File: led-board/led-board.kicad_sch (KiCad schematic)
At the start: 0 parts

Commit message: wip: start LED circuit
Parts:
- added D1: LED, symbol Device:LED
- added R1: R, symbol Device:R
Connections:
- new net: D1.2 (A), R1.1
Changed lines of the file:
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@@
 	(generator_version "10.0")
 	(paper "A4")
+	(title_block
+		(date "2026-04-19")
+		(rev "v0.0.1")
+	)
+	(wire
+		(pts
+			(xy 132.08 82.55) (xy 133.35 82.55)
+		)
+		(stroke
+			(width 0)
+			(type default)
+		)
+	)
+	(symbol
+		(lib_id "Device:R")
+		(at 137.16 82.55 90)
+		(unit 1)
+		(body_style 1)
+		(exclude_from_sim no)
+		(in_bom yes)
+		(on_board yes)
+		(in_pos_files yes)
+		(dnp no)
+		(fields_autoplaced yes)
+		(property "Reference" "R1"
+			(at 137.16 76.2 90)
+			(show_name no)
+			(do_not_autoplace no)
+			(effects
+				(font
+					(size 1.27 1.27)
+				)
+			)
+		)
+		(property "Value" "R"
+			(at 137.16 78.74 90)
+			(show_name no)
+			(do_not_autoplace no)
+			(effects
+				(font
+					(size 1.27 1.27)
+				)
+			)
+		)
+		(property "Footprint" ""
+			(at 137.16 84.328 90)
+			(hide yes)
+			(show_name no)
+			(do_not_autoplace no)
+			(effects
+				(font
+					(size 1.27 1.27)
+				)
+			)
+		)
+		(property "Datasheet" ""
+			(at 137.16 82.55 0)
+			(hide yes)
+			(show_name no)
+			(do_not_autoplace no)
+			(effects
+				(font
+					(size 1.27 1.27)
+				)
+			)
+		)
+		(property "Description" "Resistor"
+			(at 137.16 82.55 0)
+			(hide yes)
+			(show_name no)
+			(do_not_autoplace no)
+			(effects
+				(font
+					(size 1.27 1.27)
+				)
+			)
+		)
+		(pin "2"
+		)
+		(pin "1"
+		)
+		(instances
+			(project "led-board"
+				(path "/626610d0-ed57-4fcb-9775-a4b6ac83fd7f"
+					(reference "R1")
+					(unit 1)
+				)
+			)
+		)
+	)
+	(symbol
+		(lib_id "Device:LED")
+		(at 128.27 82.55 0)
+		(unit 1)
+		(body_style 1)
+		(exclude_from_sim no)
+		(in_bom yes)
+		(on_board yes)
+		(in_pos_files yes)
+		(dnp no)
+		(fields_autoplaced yes)
+		(property "Reference" "D1"
+			(at 126.6825 76.2 0)
+			(show_name no)
+			(do_not_autoplace no)
+			(effects
+				(font
+					(size 1.27 1.27)
+				)
+			)
+		)
+		(property "Value" "LED"
+			(at 126.6825 78.74 0)
+			(show_name no)
+			(do_not_autoplace no)
+			(effects
+				(font
+					(size 1.27 1.27)
+				)
+			)
+		)
+		(property "Footprint" ""
+			(at 128.27 82.55 0)
+			(hide yes)
+			(show_name no)
+			(do_not_autoplace no)
+			(effects
+				(font
+					(size 1.27 1.27)
+				)
+			)
+		)
+		(property "Datasheet" ""
+			(at 128.27 82.55 0)
+			(hide yes)
+			(show_name no)
+			(do_not_autoplace no)
+			(effects
+				(font
+					(size 1.27 1.27)
+				)
+			)
+		)
+		(property "Description" "Light emitting diode"
+			(at 128.27 82.55 0)
+			(hide yes)
+			(show_name no)
+			(do_not_autoplace no)
+			(effects
+				(font
+					(size 1.27 1.27)
+				)
+			)
+		)
+		(property "Sim.Pins" "1=K 2=A"
+			(at 128.27 82.55 0)
+			(hide yes)
+			(show_name no)
+			(do_not_autoplace no)
+			(effects
+				(font
+					(size 1.27 1.27)
+				)
+			)
+		)
+		(pin "2"
+		)
+		(pin "1"
+		)
+		(instances
+			(project "led-board"
+				(path "/626610d0-ed57-4fcb-9775-a4b6ac83fd7f"
+					(reference "D1")
+					(unit 1)
+				)
+			)
+		)
+	)
 	(sheet_instances
 		(path "/"

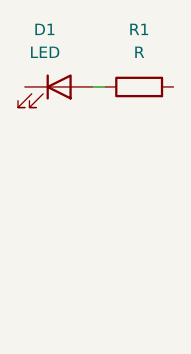
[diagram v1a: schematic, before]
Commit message: tambah 2 lampu
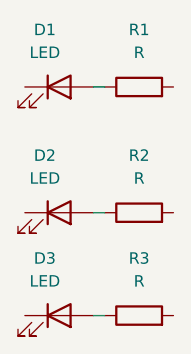
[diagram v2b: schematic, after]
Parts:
- added D2, D3: LED, symbol Device:LED
- added R2, R3: R, symbol Device:R
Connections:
- new net: D3.2 (A), R3.1
- new net: D2.2 (A), R2.1

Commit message: tambah jadi banyak lampu
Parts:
- added D10, D11, D12, D4, D5, D6, D7, D8, D9: LED, symbol Device:LED
- added R10, R11, R12, R4, R5, R6, R7, R8, R9: R, symbol Device:R
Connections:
- new net: D7.2 (A), R7.1
- new net: D5.2 (A), R5.1
- new net: D6.2 (A), R6.1
- new net: D10.2 (A), R10.1
- new net: D12.2 (A), R12.1
- new net: D8.2 (A), R8.1
- new net: D9.2 (A), R9.1
- new net: D11.2 (A), R11.1
- new net: D4.2 (A), R4.1
